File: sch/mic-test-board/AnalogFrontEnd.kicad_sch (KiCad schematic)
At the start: 0 parts

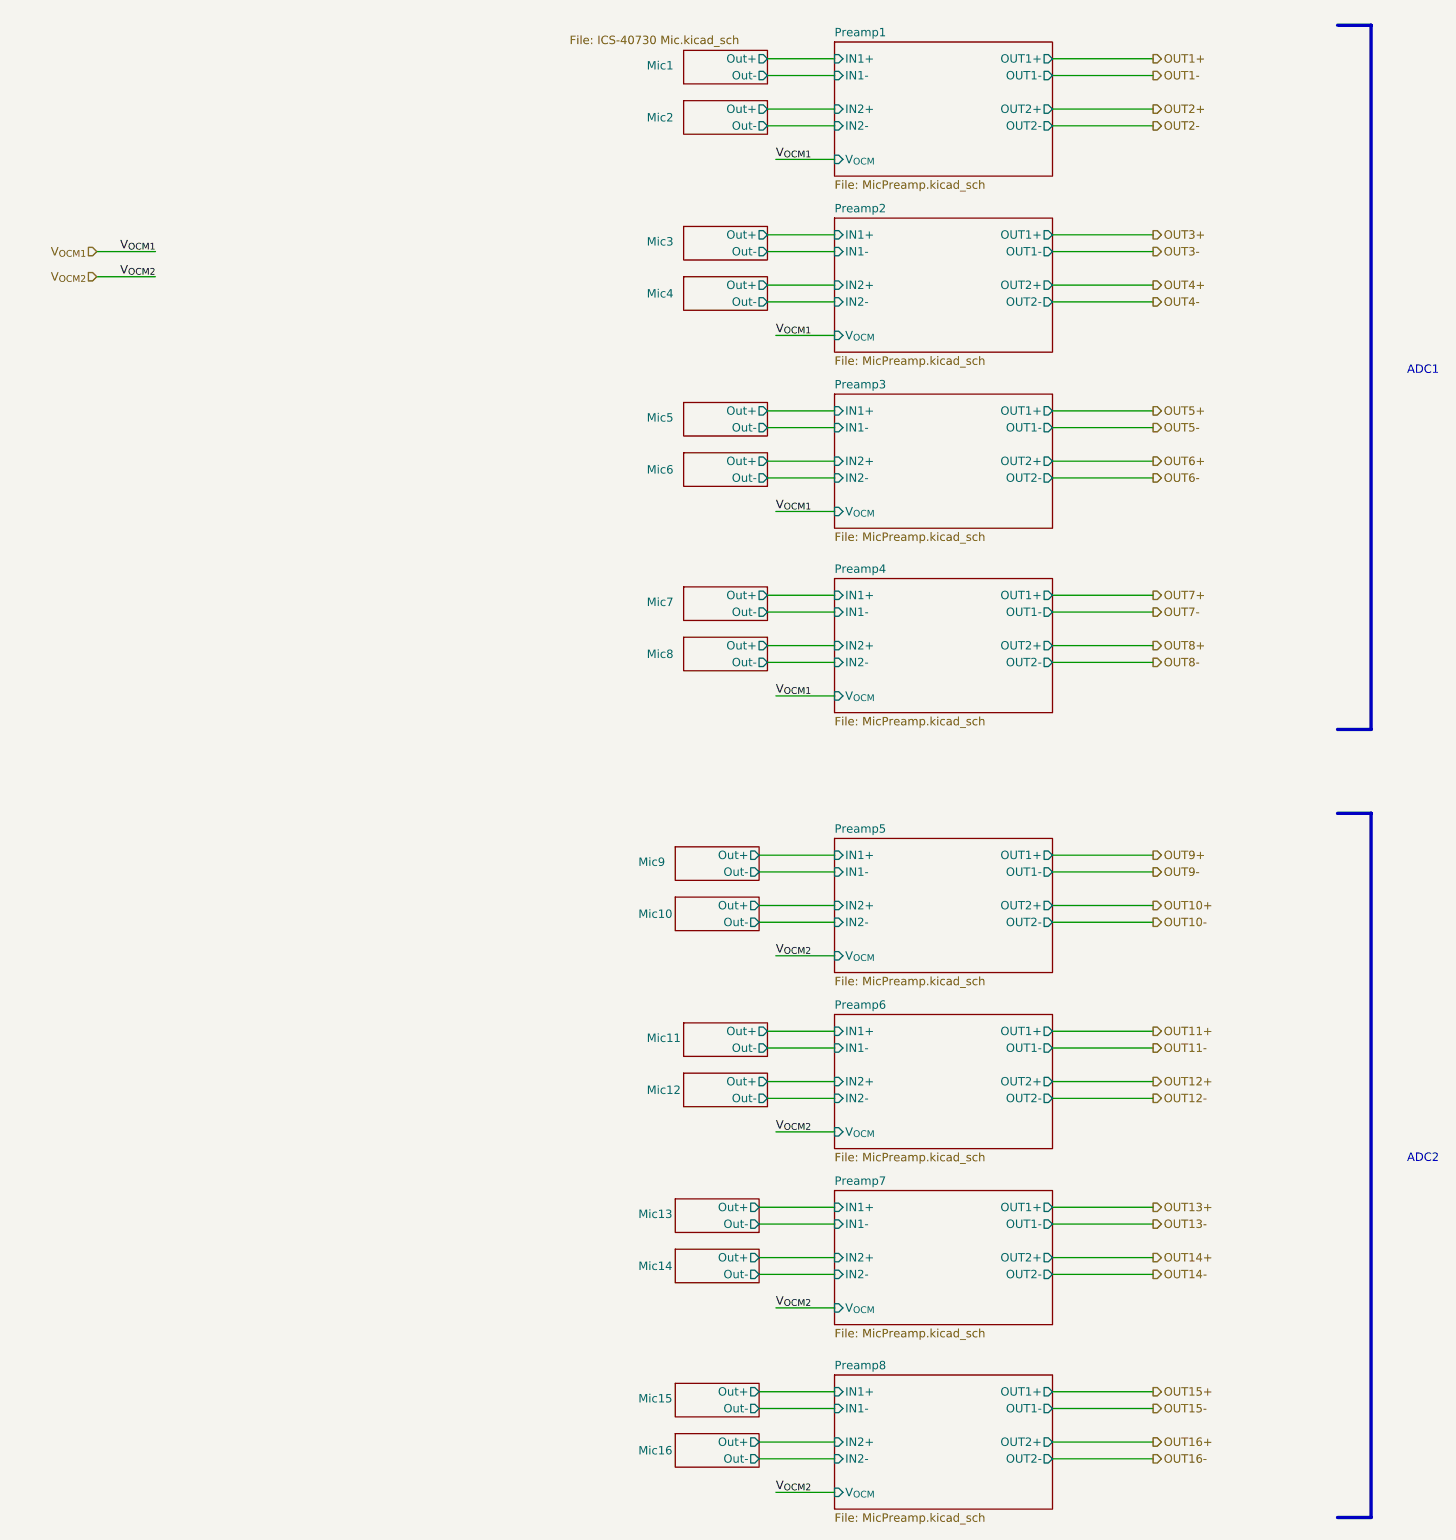
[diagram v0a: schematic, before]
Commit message: pcb: commit before large routing effort
 - schematic refactor to split preamps to each mic board
 - Mic board and main board are placed
 - no tracks laid
 - critical parts selected
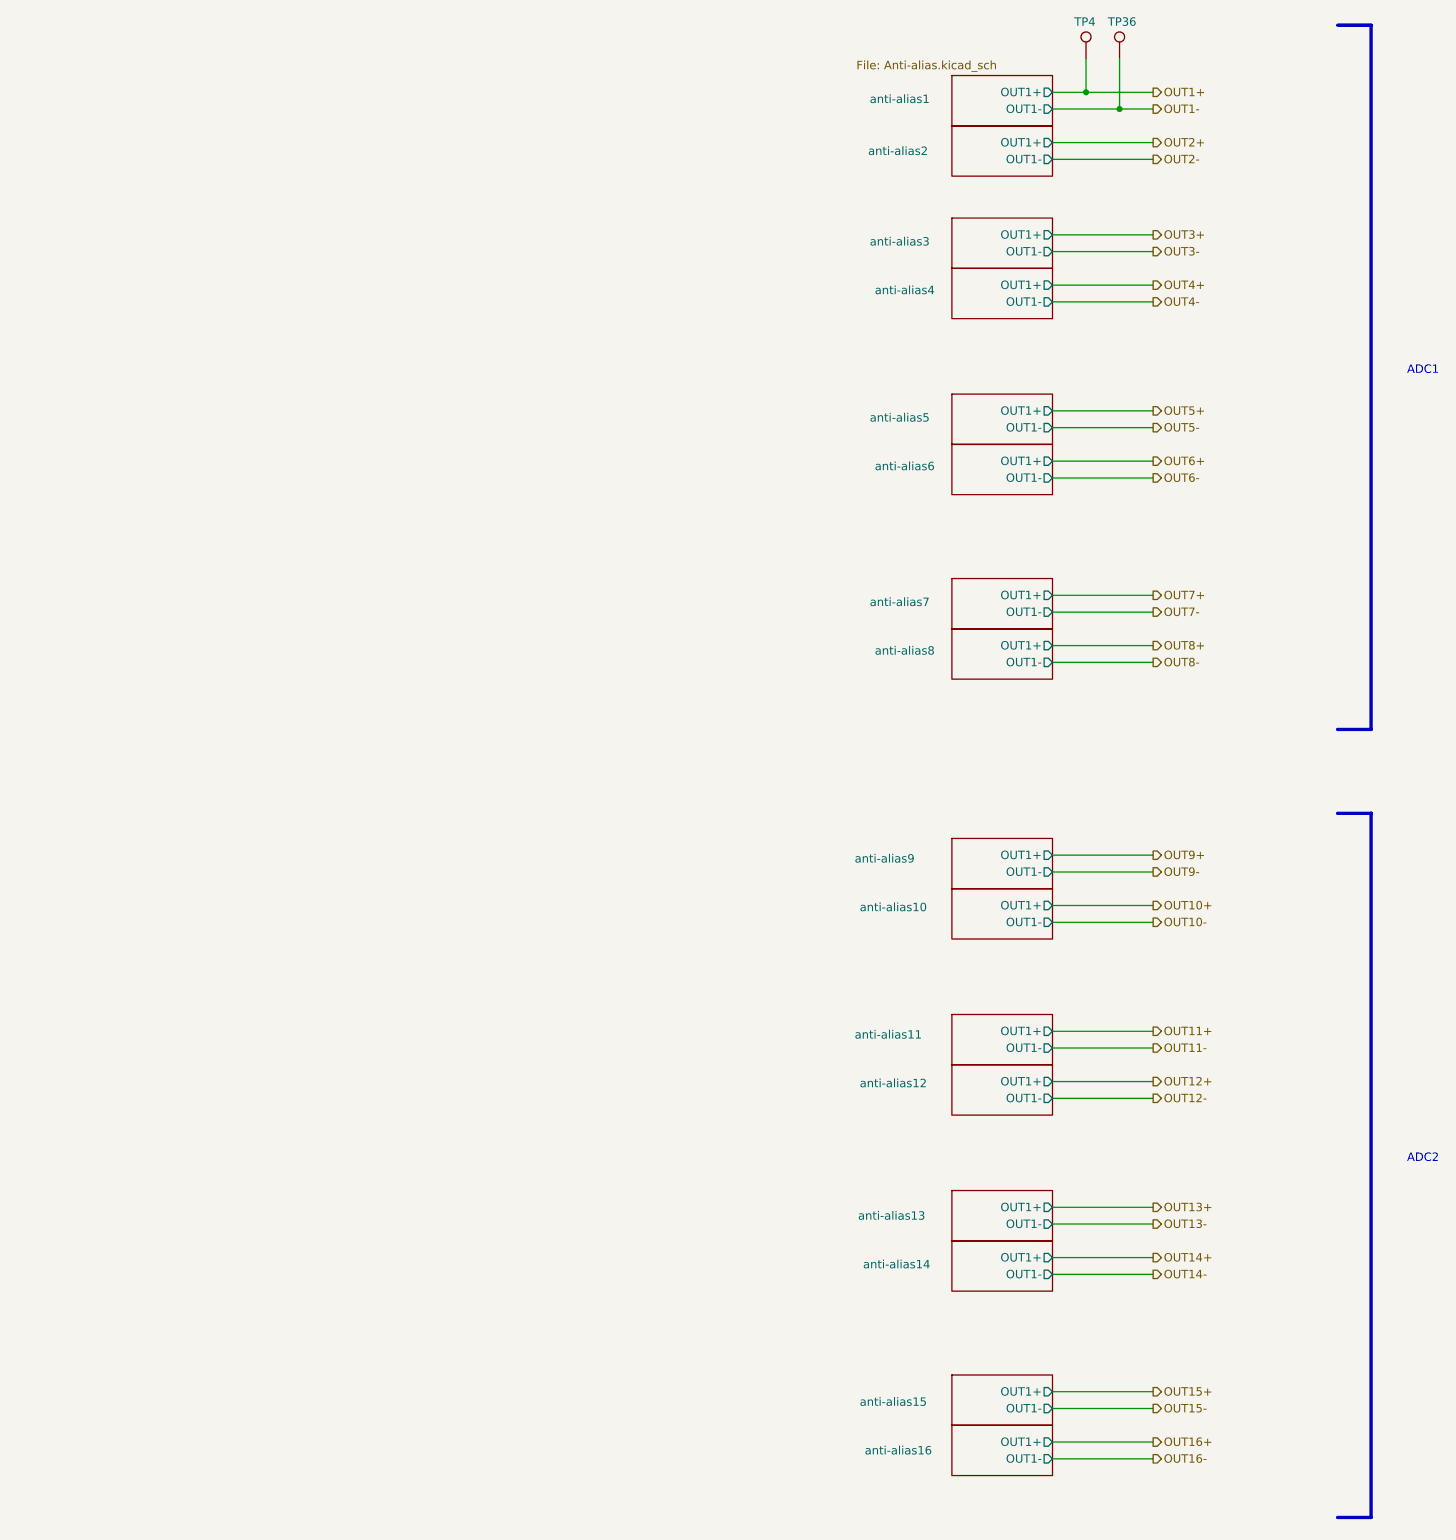
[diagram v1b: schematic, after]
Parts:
- added TP36, TP4: Hole_1.5mm, TestPoint:TestPoint_THTPad_D1.5mm_Drill0.7mm, symbol Connector:TestPoint
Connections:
- net OUT1+: now also TP4.1
- net OUT1-: now also TP36.1
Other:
- sheet Preamp1 renamed anti-alias1
- removed sheet Mic1
- removed sheet Mic10
- removed sheet Mic11
- removed sheet Mic12
- removed sheet Mic13
- removed sheet Mic14
- removed sheet Mic15
- removed sheet Mic16
- removed sheet Mic2
- removed sheet Mic3
- removed sheet Mic4
- removed sheet Mic5
- removed sheet Mic6
- removed sheet Mic7
- removed sheet Mic8
- removed sheet Mic9
- removed sheet Preamp2
- removed sheet Preamp3
- removed sheet Preamp4
- removed sheet Preamp5
- removed sheet Preamp6
- removed sheet Preamp7
- removed sheet Preamp8
- added sheet anti-alias10 (Anti-alias.kicad_sch)
- added sheet anti-alias11 (Anti-alias.kicad_sch)
- added sheet anti-alias12 (Anti-alias.kicad_sch)
- added sheet anti-alias13 (Anti-alias.kicad_sch)
- added sheet anti-alias14 (Anti-alias.kicad_sch)
- added sheet anti-alias15 (Anti-alias.kicad_sch)
- added sheet anti-alias16 (Anti-alias.kicad_sch)
- added sheet anti-alias2 (Anti-alias.kicad_sch)
- added sheet anti-alias3 (Anti-alias.kicad_sch)
- added sheet anti-alias4 (Anti-alias.kicad_sch)
- added sheet anti-alias5 (Anti-alias.kicad_sch)
- added sheet anti-alias6 (Anti-alias.kicad_sch)
- added sheet anti-alias7 (Anti-alias.kicad_sch)
- added sheet anti-alias8 (Anti-alias.kicad_sch)
- added sheet anti-alias9 (Anti-alias.kicad_sch)
- sheet anti-alias1: file MicPreamp.kicad_sch -> Anti-alias.kicad_sch
- sheet anti-alias1 ports: added none; removed IN1+, IN1-, IN2+, IN2-, OUT2+, OUT2-, V_{OCM}
- company: (none) -> Josh Berry
- title: (none) -> Sound Compass POC

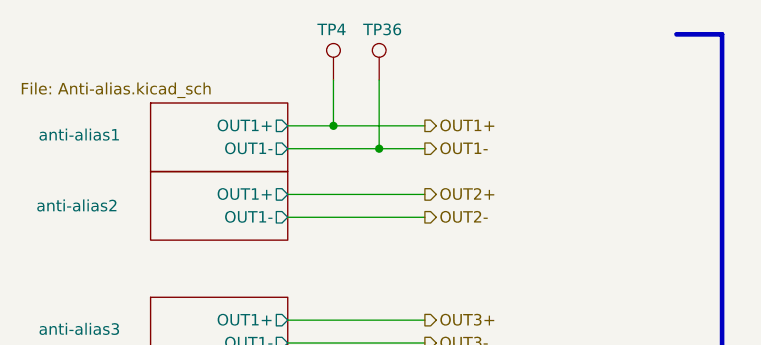
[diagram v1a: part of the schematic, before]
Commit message: pcb: finished routing mic board and ADC board.
 - BOM complete
 - uController pinout configured with CubeMX and re-checked
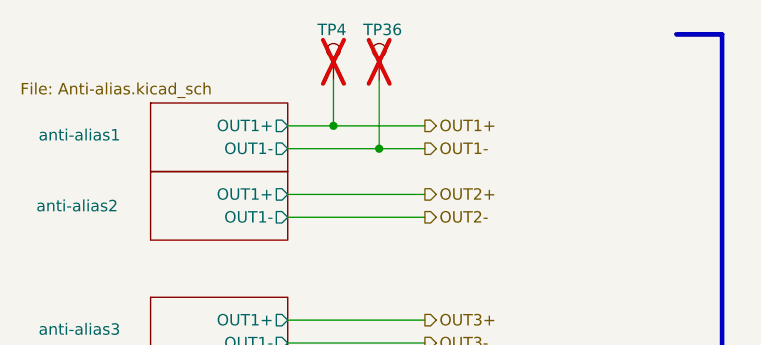
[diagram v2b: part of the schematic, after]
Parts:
- TP36, TP4: now not fitted
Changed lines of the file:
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@@
 		(in_bom yes)
 		(on_board yes)
-		(dnp no)
+		(dnp yes)
 		(property "Reference" "TP36"
 			(at 211.582 24.892 0)
@@
 		(in_bom yes)
 		(on_board yes)
-		(dnp no)
+		(dnp yes)
 		(property "Reference" "TP4"
 			(at 206.502 24.892 0)

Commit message: pcb: ordered PCB's and BOM! RevA and v240506
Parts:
- TP36, TP4: now fitted; now left out of the parts list
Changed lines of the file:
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@@
 		(unit 1)
 		(exclude_from_sim no)
-		(in_bom yes)
+		(in_bom no)
 		(on_board yes)
-		(dnp yes)
+		(dnp no)
 		(property "Reference" "TP36"
 			(at 211.582 24.892 0)
@@
 			)
 		)
-		(property "Supplier Number" ""
+		(property "Supplier Number" "~"
 			(at 213.36 30.48 0)
 			(effects
@@
 		(unit 1)
 		(exclude_from_sim no)
-		(in_bom yes)
+		(in_bom no)
 		(on_board yes)
-		(dnp yes)
+		(dnp no)
 		(property "Reference" "TP4"
 			(at 206.502 24.892 0)
@@
 			)
 		)
-		(property "Supplier Number" ""
+		(property "Supplier Number" "~"
 			(at 208.28 30.48 0)
 			(effects
